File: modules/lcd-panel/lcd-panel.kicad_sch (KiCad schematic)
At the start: 9 parts, among them J1 5051100692, J2 5051104091, U1 LP8556SQ-E09/NOPB

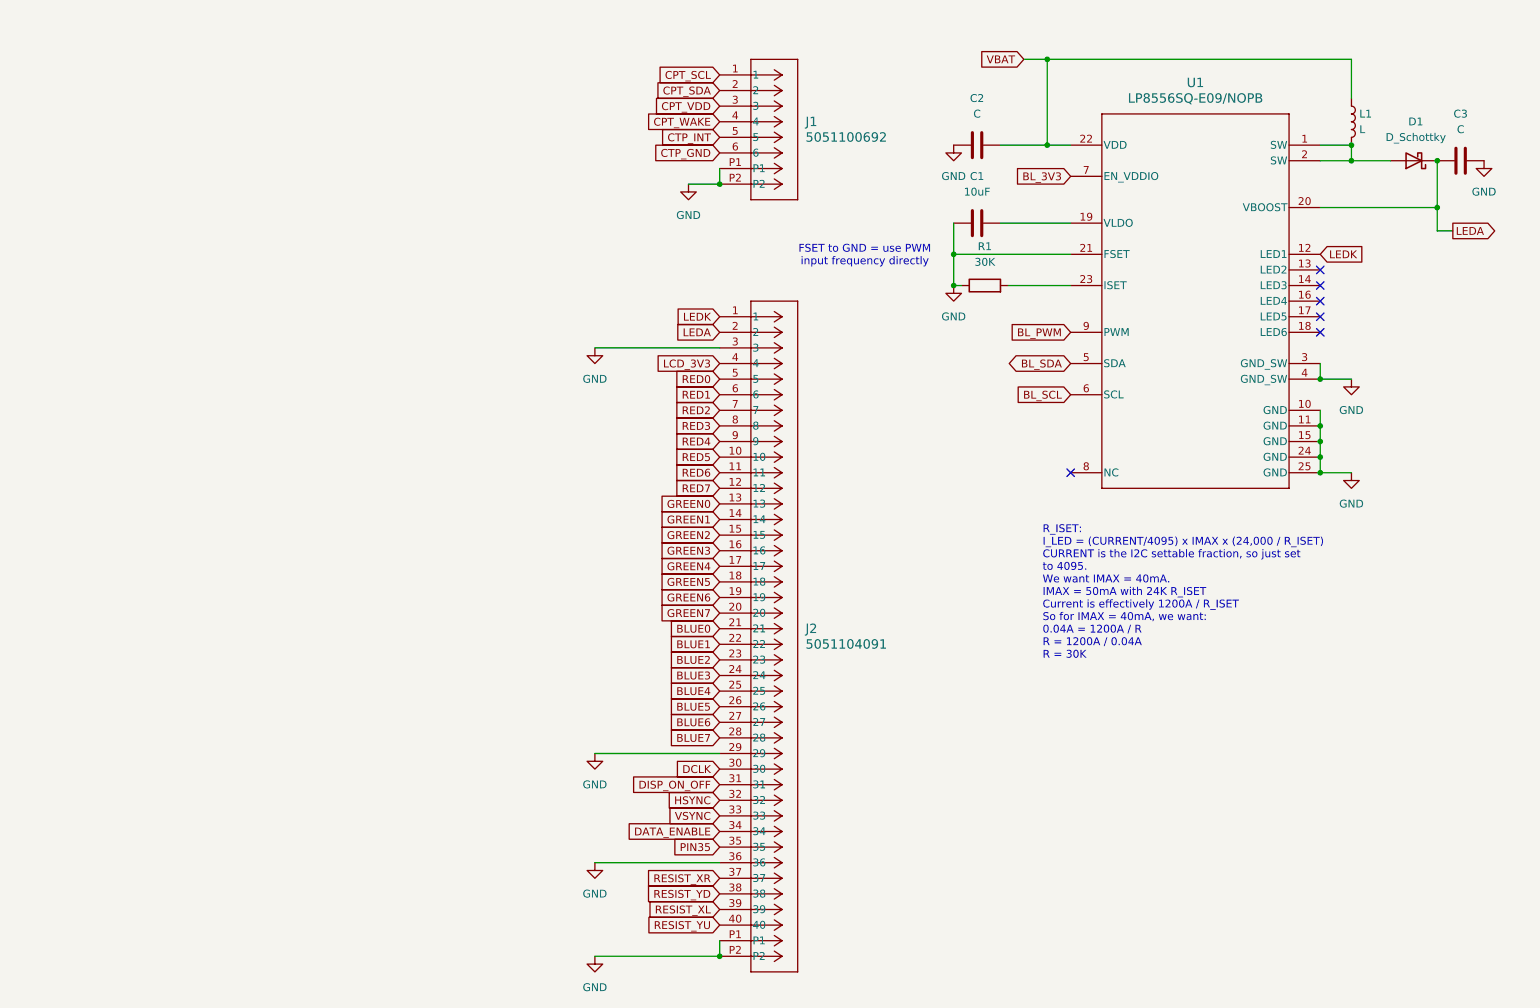
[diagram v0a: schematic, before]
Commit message: Finish LCD - updating projects
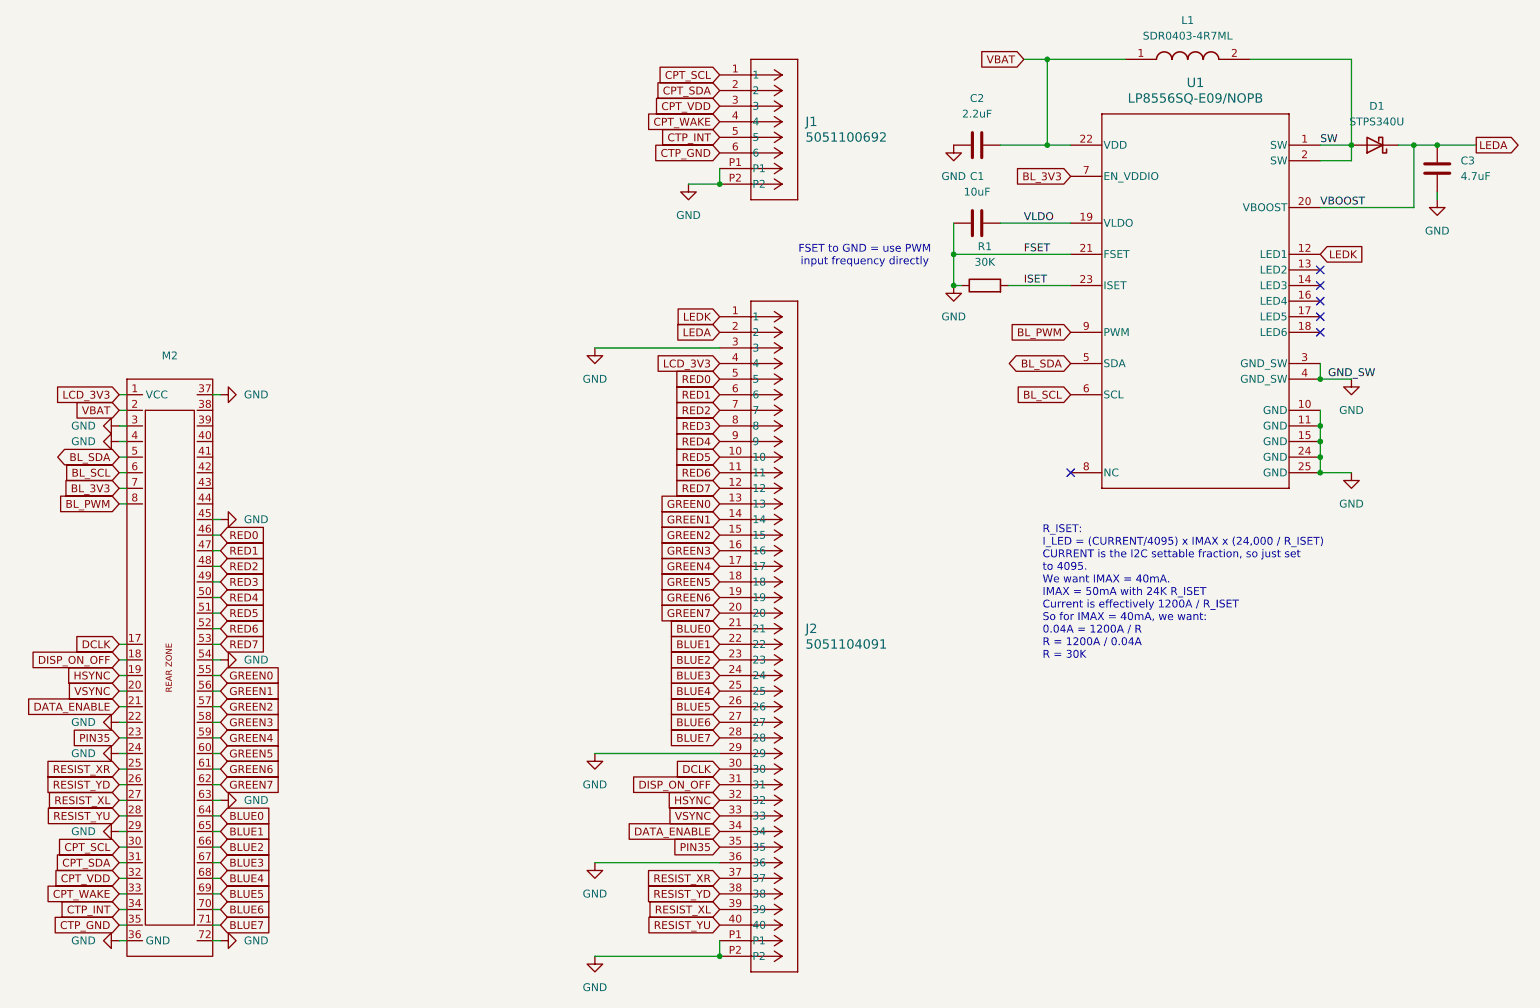
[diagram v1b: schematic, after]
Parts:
- removed L1: L, symbol Device:L
- added L1: SDR0403-4R7ML, lcd-panel:SDR0403, symbol SDR0403-4R7ML:SDR0403-4R7ML
- added M2: ~, MegaCastle:MegaCastle2x36-Module-I40.0x86.6-MFFFFFFFFFFFFFF-SPAREPAD, symbol MegaCastle:MegaCastle2x36-Module-I40.0x86.6-MFFFFFFFFFFFFFF
- C1: footprint (none) -> Capacitor_SMD:C_0603_1608Metric_Pad1.08x0.95mm_HandSolder
- C2: value C -> 2.2uF; footprint (none) -> Capacitor_SMD:C_0603_1608Metric_Pad1.08x0.95mm_HandSolder
- C3: value C -> 4.7uF; footprint (none) -> Capacitor_SMD:C_0603_1608Metric_Pad1.08x0.95mm_HandSolder
- D1: value D_Schottky -> STPS340U; footprint (none) -> Diode_SMD:D_SOD-123
- R1: footprint (none) -> Resistor_SMD:R_0603_1608Metric_Pad0.98x0.95mm_HandSolder
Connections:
- net BLUE0: now also M2.64
- net BLUE1: now also M2.65
- net BLUE2: now also M2.66
- net BLUE3: now also M2.67
- net BLUE4: now also M2.68
- net BLUE5: now also M2.69
- net BLUE6: now also M2.70
- net BLUE7: now also M2.71
- net BL_3V3: now also M2.7
- net BL_PWM: now also M2.8
- net BL_SCL: now also M2.6
- net BL_SDA: now also M2.5
- net CPT_SCL: now also M2.30
- net CPT_SDA: now also M2.31
- net CPT_VDD: now also M2.32
- net CPT_WAKE: now also M2.33
- net CTP_GND: now also M2.35
- net CTP_INT: now also M2.34
- net DATA_ENABLE: now also M2.21
- net DCLK: now also M2.17
- net DISP_ON_OFF: now also M2.18
- net GND: now also M2.22, M2.24, M2.29, M2.3, M2.36 (GND), M2.37, M2.4, M2.45, M2.54, M2.63, M2.72
- net GREEN0: now also M2.55
- net GREEN1: now also M2.56
- net GREEN2: now also M2.57
- net GREEN3: now also M2.58
- net GREEN4: now also M2.59
- net GREEN5: now also M2.60
- net GREEN6: now also M2.61
- net GREEN7: now also M2.62
- net HSYNC: now also M2.19
- net LCD_3V3: now also M2.1 (VCC)
- net PIN35: now also M2.23
- net RED0: now also M2.46
- net RED1: now also M2.47
- net RED2: now also M2.48
- net RED3: now also M2.49
- net RED4: now also M2.50
- net RED5: now also M2.51
- net RED6: now also M2.52
- net RED7: now also M2.53
- net RESIST_XL: now also M2.27
- net RESIST_XR: now also M2.25
- net RESIST_YD: now also M2.26
- net RESIST_YU: now also M2.28
- net VBAT: now also L1.1, M2.2
- net VSYNC: now also M2.20
- net VLDO: now reaches C1.2, U1.19 (VLDO)
- net ISET: now reaches R1.2, U1.23 (ISET)
- net SW: now reaches D1.2 (A), U1.1 (SW), U1.2 (SW)
- net SW: now also L1.2
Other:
- moved on the sheet: C3, D1
